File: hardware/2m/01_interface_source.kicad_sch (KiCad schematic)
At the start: 24 parts, among them J101 Controller 20 pin, U101 TPS22919DCKR, U102 SN74LVC2G66DCUR, U103 Si5351A-B-GT, Y101 25MHz CL10p 10/10ppm

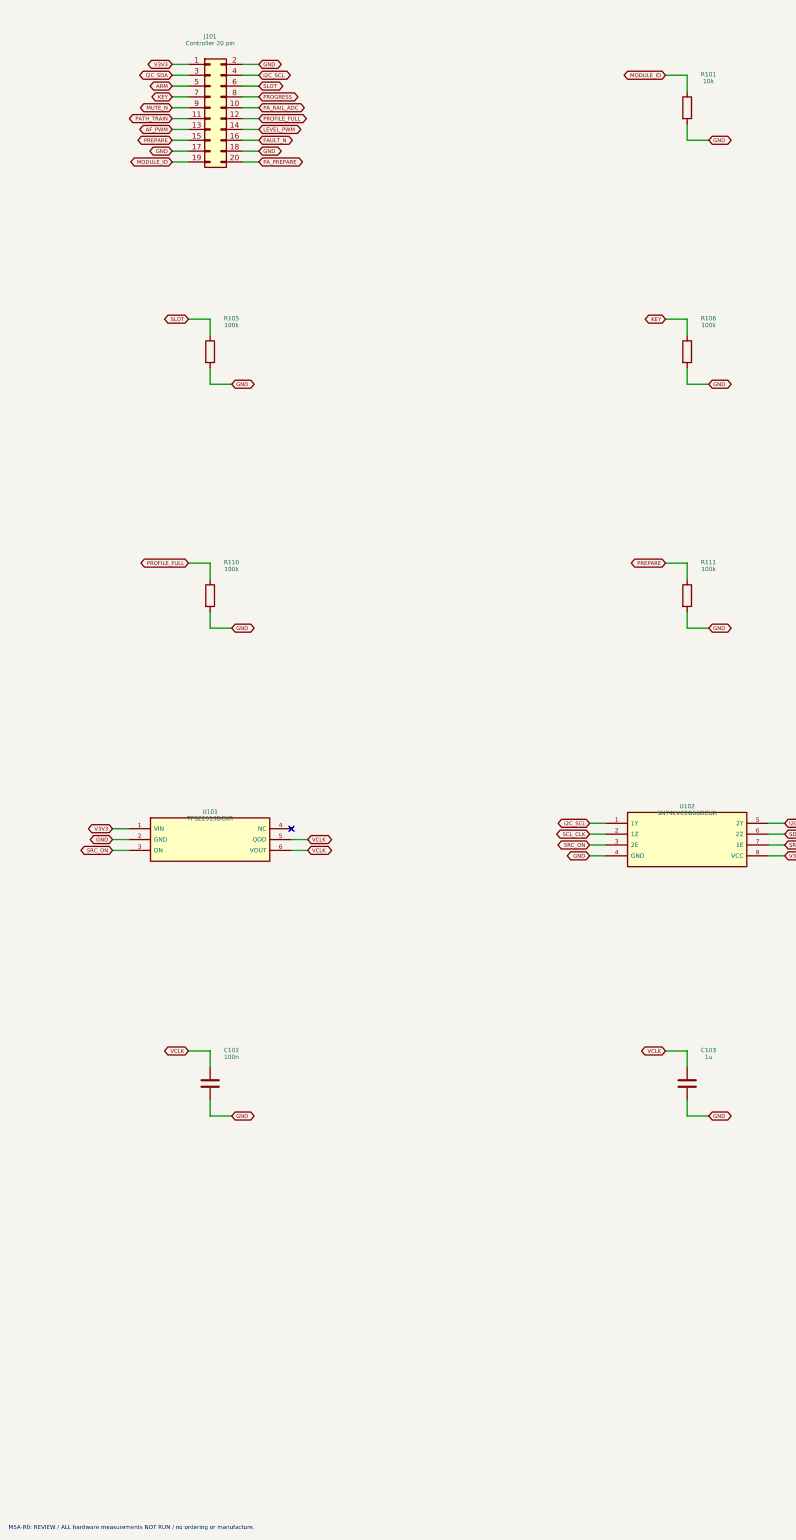
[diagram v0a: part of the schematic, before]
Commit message: Preserve M5A-R1 VHF electrical candidate and review evidence
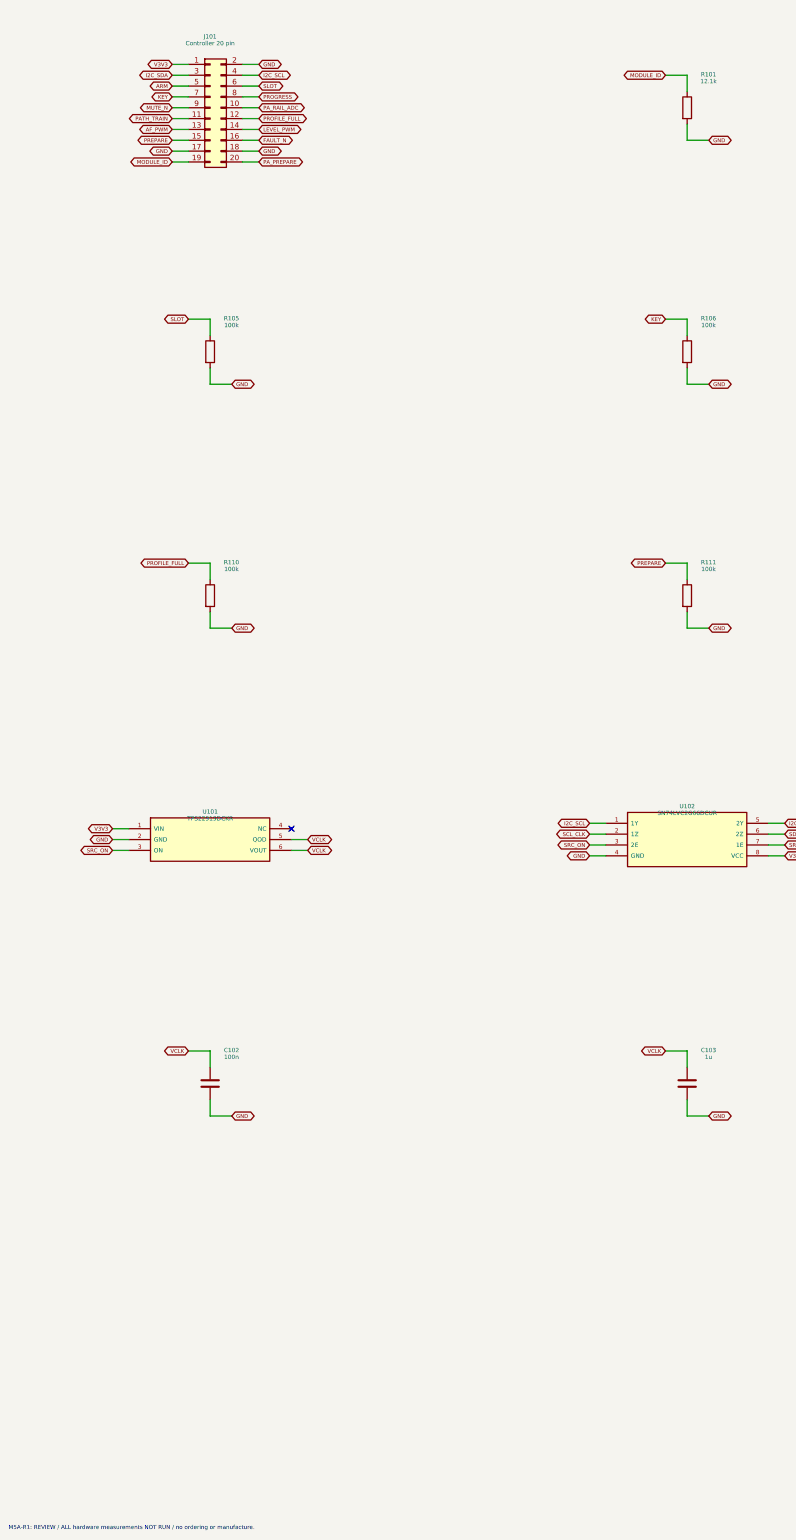
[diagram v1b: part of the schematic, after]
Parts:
- R101: value 10k -> 12.1k; MPN RC0603FR-0710KL -> RC0603FR-0712K1L; Variant_BUCK4S_Value 22k -> 27.4k
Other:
- note added: "M5A-R1: REVIEW / ALL hardware measurements NOT RUN / no ordering or manufacture."
- note removed: "M5A-R0: REVIEW / ALL hardware measurements NOT RUN / no ordering or manufacture."

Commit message: Preserve M5A-R3 historical transmitter schematic and review
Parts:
- R101: value 12.1k -> 15k; Engineering_Note (none) -> R3 distinct passive ID:15k2S,33.2k4S,75ktraining. Do not ar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; MPN RC0603FR-0712K1L -> RC0603FR-0715KL; Variant_BUCK4S_Value 27.4k -> 33.2k; Variant_TRAIN_ONLY_Value 47k -> 75k
- U103: Engineering_Note Divide-by-6 MS0 and MS2, shared PLL 6*f; CLK1 disabled. Int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 -> R3: PLL_A=6*desired RF; MS0=12 -> RF/2 for retained DL3BBX 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
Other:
- note added: "M5A-R3: REVIEW / ALL hardware measurements NOT RUN / no ordering or manufacture."
- note added: "R3: no RF/analog/thermal hardware validation. Original RF attribution and open procurement in M5A_R3 documents."
- note removed: "144.5-144.9 MHz championship; other channels only under valid country profile. SCL activity clears ARM. Source supply/bus isolated when off. No RF claims until spectrum measurements."
- note removed: "M5A-R1: REVIEW / ALL hardware measurements NOT RUN / no ordering or manufacture."

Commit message: Preserve M5A-R4 economical VHF electrical review baseline
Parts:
- R101: value 15k -> 18.2k; Engineering_Note R3 distinct passive ID:15k2S,33.2k4S,75ktraining. Do not ar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 -> R4-only IDs18.2k2S/39.2k4S/82ktrain. Bind calibration/firmw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; MPN RC0603FR-0715KL -> RC0603FR-0718K2L; Variant_BUCK4S_Value 33.2k -> 39.2k; Variant_TRAIN_ONLY_Value 75k -> 82k
- U103: Engineering_Note R3: PLL_A=6*desired RF; MS0=12 -> RF/2 for retained DL3BBX 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 -> R4 PLL_A=6*fRF, both MS0 and MS2 divide6; CLK1 disabled. Lo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
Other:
- note added: "M5A-R4: REVIEW / ALL hardware measurements NOT RUN / no ordering or manufacture."
- note added: "M5A-R4: hardware measurements NOT_RUN; source/reference and simplification in R4 documents."
- note removed: "M5A-R3: REVIEW / ALL hardware measurements NOT RUN / no ordering or manufacture."
- note removed: "R3: no RF/analog/thermal hardware validation. Original RF attribution and open procurement in M5A_R3 documents."

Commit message: Preserve M5B-E1 integrated RF2M evaluation baseline
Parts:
- J101: footprint Connector_IDC:IDC-Header_2x10_P2.54mm_Vertical -> ARDF_2M:WR_BHD_61202021621; Engineering_Note Controller input maximum 3.465V; power/ground sequencing in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 -> WR-BHD20pin2.54 pitch,33.06mm body9.1mm width8.75mm height;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; MPN OPEN keyed 20pin 2.54mm -> 61202021621
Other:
- note added: "M5B-E1 / integrated evaluation PCB / NOT RELEASED / hardware tests NOT_RUN"
- note added: "M5B-E1: REVIEW / ALL hardware measurements NOT RUN / no ordering or manufacture."
- note removed: "M5A-R4: REVIEW / ALL hardware measurements NOT RUN / no ordering or manufacture."
- note removed: "M5A-R4: hardware measurements NOT_RUN; source/reference and simplification in R4 documents."

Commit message: Implement M5B-E3 standard JLCPCB RF2M evaluation board
Recalculate and implement 1.6 mm / 1 oz RF geometry, power copper, thermal vias, connector holes and manufacturing legend. Preserve electrical functions and population variants. Add native-geometry DFM, regression checks and fresh native/fabrication review archives. CAD milestone only; no manufacturing or operational release.
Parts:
- C101, C102: footprint Capacitor_SMD:C_0603_1608Metric -> ARDF_2M:C_0603_1608Metric_E3
- C103: footprint Capacitor_SMD:C_0805_2012Metric -> ARDF_2M:C_0805_2012Metric_E3
- J101: Engineering_Note WR-BHD20pin2.54 pitch,33.06mm body9.1mm width8.75mm height;drawing002.00130Aug2026. Local version of IDC pattern has1.1mm drills and manufacturer body envelope. -> WR-BHD20pin2.54 pitch,33.06mm body9.1mm width8.75mm height;drawing002.00130Aug2026. Local version of IDC pattern has1.30mm drills and manufacturer body envelope. E3:1.30mmfinishedhole/1.90mmland. WEmax0.79mmsquarelead diagonal1.117mm;JLCminhole1.22mm. Tailmin2.85mmminusboardmax1.76mm=1.09mmprotrusion.
- R101, R102, R103, R104, R105, R106, R107, R108, R109, R110, R111, R112, R115, R116: footprint Resistor_SMD:R_0603_1608Metric -> ARDF_2M:R_0603_1608Metric_E3
- TP101, TP102: footprint TestPoint:TestPoint_Pad_D1.0mm -> ARDF_2M:TestPoint_Pad_D1.0mm_E3
- U101: footprint Package_TO_SOT_SMD:SOT-363_SC-70-6 -> ARDF_2M:SOT-363_SC-70-6_E3
- U102: footprint Package_SO:VSSOP-8_2.3x2mm_P0.5mm -> ARDF_2M:VSSOP-8_2.3x2mm_P0.5mm_E3
- U103: footprint Package_SO:MSOP-10_3x3mm_P0.5mm -> ARDF_2M:MSOP-10_3x3mm_P0.5mm_E3
- Y101: footprint Crystal:Crystal_SMD_3225-4Pin_3.2x2.5mm -> ARDF_2M:Crystal_SMD_3225-4Pin_3.2x2.5mm_E3
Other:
- note added: "M5B-E3 / integrated evaluation PCB / NOT RELEASED / hardware tests NOT_RUN"
- note added: "M5B-E3: REVIEW / ALL hardware measurements NOT RUN / no ordering or manufacture."
- note removed: "M5B-E1 / integrated evaluation PCB / NOT RELEASED / hardware tests NOT_RUN"
- note removed: "M5B-E1: REVIEW / ALL hardware measurements NOT RUN / no ordering or manufacture."

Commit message: Implement M5B-E4 thermal candidate with source-joint assembly hold
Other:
- note added: "M5B-E4 / integrated evaluation PCB / NOT RELEASED / hardware tests NOT_RUN"
- note added: "M5B-E4: REVIEW / ALL hardware measurements NOT RUN / no ordering or manufacture."
- note removed: "M5B-E3 / integrated evaluation PCB / NOT RELEASED / hardware tests NOT_RUN"
- note removed: "M5B-E3: REVIEW / ALL hardware measurements NOT RUN / no ordering or manufacture."

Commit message: Implement M5B-E4R1 source-joint prototype candidate
Replace source mask islands with a controlled open-via hybrid and native-derived local stencil. Preserve standard JLCPCB and RF circuitry. Add assembly qualification, thermal convergence and adverse sensitivities, native DFM/mutation checks and fresh review exports. Conservative 110 C target is missed; 125 C physical gate stays open. No acceptance tag or manufacturing authorization.
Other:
- note added: "M5B-E4R1R1R1 / integrated evaluation PCB / NOT RELEASED / hardware tests NOT_RUN"
- note added: "M5B-E4R1R1R1: REVIEW / ALL hardware measurements NOT RUN / no ordering or manufacture."
- note removed: "M5B-E4 / integrated evaluation PCB / NOT RELEASED / hardware tests NOT_RUN"
- note removed: "M5B-E4: REVIEW / ALL hardware measurements NOT RUN / no ordering or manufacture."

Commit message: M5B-E5: compact RF2M to the shared 150x110 mm platform
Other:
- note added: "M5B-E5R1R1 / integrated evaluation PCB / NOT RELEASED / hardware tests NOT_RUN"
- note added: "M5B-E5R1R1: REVIEW / ALL hardware measurements NOT RUN / no ordering or manufacture."
- note removed: "M5B-E4R1R1R1 / integrated evaluation PCB / NOT RELEASED / hardware tests NOT_RUN"
- note removed: "M5B-E4R1R1R1: REVIEW / ALL hardware measurements NOT RUN / no ordering or manufacture."
